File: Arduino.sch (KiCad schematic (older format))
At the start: 0 parts

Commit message: Arduino
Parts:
- added ARD?: ARDUINO_PINS, ~, symbol ARDUINO_PINS
- added R? (x13): R, ~, symbol R
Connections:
- net labels added: ADC_CS_N, CURR_MEAS, DAC_CS_N, GND, LED_EN_PWM, RELAY+, RELAY-, V+ADJ_MON, V-ADJ_MON
- net labels removed: CS_N, LED_EN, LED_FREQ, Relay+, Relay-
- wire segments 0 -> 27

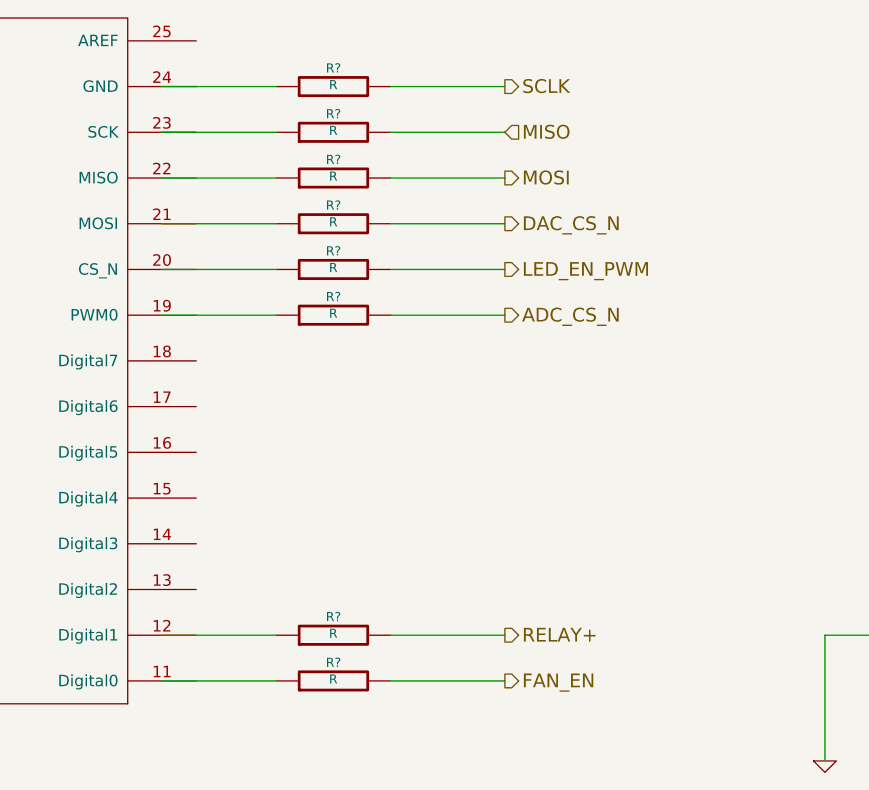
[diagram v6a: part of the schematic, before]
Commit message: Fan/Power refactoring
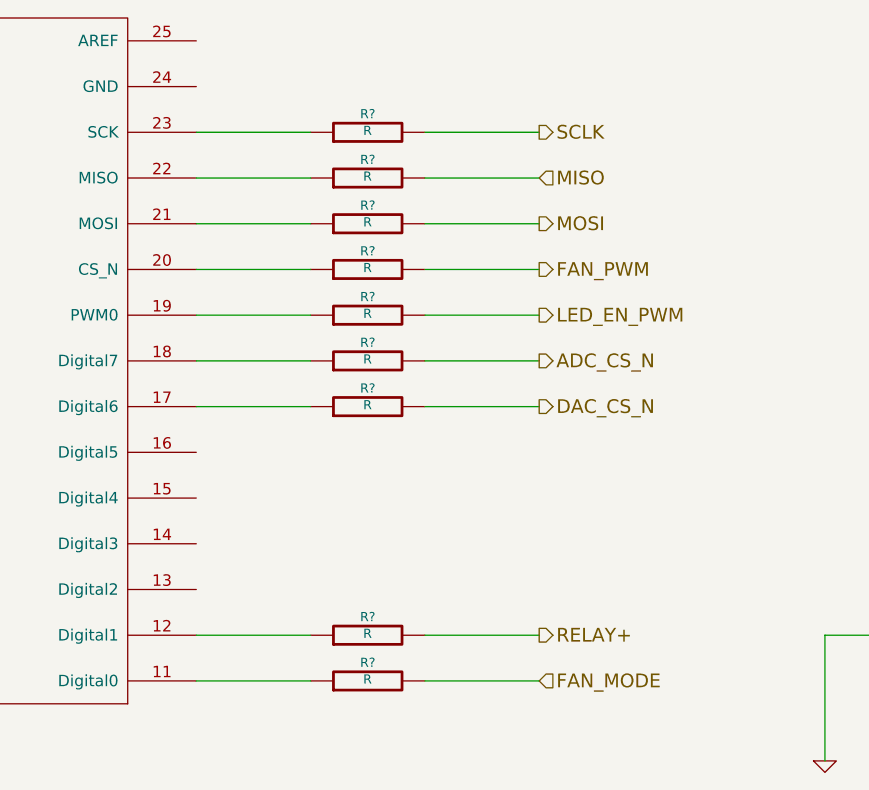
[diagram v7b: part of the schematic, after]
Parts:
- added R?: R, ~, symbol R
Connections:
- net labels added: FAN_MODE, FAN_PWM
- net labels removed: FAN_EN
- wire segments 27 -> 29
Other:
- moved on the sheet: R?
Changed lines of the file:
@@
 Comment4 ""
 $EndDescr
-Text HLabel 7450 3450 2    60   Output ~ 0
+Text HLabel 7600 3650 2    60   Output ~ 0
 MOSI
-Text HLabel 7450 3250 2    60   Input ~ 0
+Text HLabel 7600 3450 2    60   Input ~ 0
 MISO
-Text HLabel 7450 3050 2    60   Output ~ 0
+Text HLabel 7600 3250 2    60   Output ~ 0
 SCLK
-Text HLabel 7450 5450 2    60   Output ~ 0
+Text HLabel 7600 5450 2    60   Output ~ 0
 RELAY+
 Text HLabel 9900 5450 2    60   Output ~ 0
 RELAY-
-Text HLabel 7450 3650 2    60   Output ~ 0
-DAC_CS_N
-Text HLabel 7450 5650 2    60   Output ~ 0
-FAN_EN
+Text HLabel 7600 3850 2    60   Output ~ 0
+FAN_PWM
 Text HLabel 2850 5250 0    60   Input ~ 0
 TACH_MEAS
@@
 L R R?
 U 1 1 52F7405F
-P 6700 5650
-F 0 "R?" V 6780 5650 40  0000 C CNN
-F 1 "R" V 6707 5651 40  0000 C CNN
-F 2 "~" V 6630 5650 30  0000 C CNN
-F 3 "~" H 6700 5650 30  0000 C CNN
-	1    6700 5650
-	0    -1   -1   0
-$EndComp
-Wire Wire Line
-	5950 5650 6450 5650
-Wire Wire Line
-	6950 5650 7450 5650
+P 6850 5650
+F 0 "R?" V 6930 5650 40  0000 C CNN
+F 1 "R" V 6857 5651 40  0000 C CNN
+F 2 "~" V 6780 5650 30  0000 C CNN
+F 3 "~" H 6850 5650 30  0000 C CNN
+	1    6850 5650
+	0    -1   -1   0
+$EndComp
+Wire Wire Line
+	6100 5650 6600 5650
+Wire Wire Line
+	7100 5650 7600 5650
 $Comp
 L R R?
 U 1 1 52F742D4
-P 6700 5450
-F 0 "R?" V 6780 5450 40  0000 C CNN
-F 1 "R" V 6707 5451 40  0000 C CNN
-F 2 "~" V 6630 5450 30  0000 C CNN
-F 3 "~" H 6700 5450 30  0000 C CNN
-	1    6700 5450
-	0    -1   -1   0
-$EndComp
-Wire Wire Line
-	5950 5450 6450 5450
-Wire Wire Line
-	6950 5450 7450 5450
+P 6850 5450
+F 0 "R?" V 6930 5450 40  0000 C CNN
+F 1 "R" V 6857 5451 40  0000 C CNN
+F 2 "~" V 6780 5450 30  0000 C CNN
+F 3 "~" H 6850 5450 30  0000 C CNN
+	1    6850 5450
+	0    -1   -1   0
+$EndComp
+Wire Wire Line
+	6100 5450 6600 5450
+Wire Wire Line
+	7100 5450 7600 5450
 $Comp
 L R R?
@@
 L R R?
 U 1 1 52F75679
-P 6700 3050
-F 0 "R?" V 6780 3050 40  0000 C CNN
-F 1 "R" V 6707 3051 40  0000 C CNN
-F 2 "~" V 6630 3050 30  0000 C CNN
-F 3 "~" H 6700 3050 30  0000 C CNN
-	1    6700 3050
+P 6850 3250
+F 0 "R?" V 6930 3250 40  0000 C CNN
+F 1 "R" V 6857 3251 40  0000 C CNN
+F 2 "~" V 6780 3250 30  0000 C CNN
+F 3 "~" H 6850 3250 30  0000 C CNN
+	1    6850 3250
 	0    -1   -1   0
 $EndComp
@@
 L R R?
 U 1 1 52F75688
-P 6700 3250
-F 0 "R?" V 6780 3250 40  0000 C CNN
-F 1 "R" V 6707 3251 40  0000 C CNN
-F 2 "~" V 6630 3250 30  0000 C CNN
-F 3 "~" H 6700 3250 30  0000 C CNN
-	1    6700 3250
+P 6850 3450
+F 0 "R?" V 6930 3450 40  0000 C CNN
+F 1 "R" V 6857 3451 40  0000 C CNN
+F 2 "~" V 6780 3450 30  0000 C CNN
+F 3 "~" H 6850 3450 30  0000 C CNN
+	1    6850 3450
 	0    -1   -1   0
 $EndComp
@@
 L R R?
 U 1 1 52F75697
-P 6700 3450
-F 0 "R?" V 6780 3450 40  0000 C CNN
-F 1 "R" V 6707 3451 40  0000 C CNN
-F 2 "~" V 6630 3450 30  0000 C CNN
-F 3 "~" H 6700 3450 30  0000 C CNN
-	1    6700 3450
+P 6850 3650
+F 0 "R?" V 6930 3650 40  0000 C CNN
+F 1 "R" V 6857 3651 40  0000 C CNN
+F 2 "~" V 6780 3650 30  0000 C CNN
+F 3 "~" H 6850 3650 30  0000 C CNN
+	1    6850 3650
 	0    -1   -1   0
 $EndComp
@@
 L R R?
 U 1 1 52F756A6
-P 6700 3650
-F 0 "R?" V 6780 3650 40  0000 C CNN
-F 1 "R" V 6707 3651 40  0000 C CNN
-F 2 "~" V 6630 3650 30  0000 C CNN
-F 3 "~" H 6700 3650 30  0000 C CNN
-	1    6700 3650
-	0    -1   -1   0
-$EndComp
-Wire Wire Line
-	5950 3050 6450 3050
-Wire Wire Line
-	6950 3050 7450 3050
-Wire Wire Line
-	5950 3250 6450 3250
-Wire Wire Line
-	6950 3250 7450 3250
-Wire Wire Line
-	5950 3450 6450 3450
-Wire Wire Line
-	6950 3450 7450 3450
-Wire Wire Line
-	5950 3650 6450 3650
-Wire Wire Line
-	6950 3650 7450 3650
-Text HLabel 7450 3850 2    60   Output ~ 0
+P 6850 3850
+F 0 "R?" V 6930 3850 40  0000 C CNN
+F 1 "R" V 6857 3851 40  0000 C CNN
+F 2 "~" V 6780 3850 30  0000 C CNN
+F 3 "~" H 6850 3850 30  0000 C CNN
+	1    6850 3850
+	0    -1   -1   0
+$EndComp
+Wire Wire Line
+	6100 3250 6600 3250
+Wire Wire Line
+	7100 3250 7600 3250
+Wire Wire Line
+	6100 3450 6600 3450
+Wire Wire Line
+	7100 3450 7600 3450
+Wire Wire Line
+	6100 3650 6600 3650
+Wire Wire Line
+	7100 3650 7600 3650
+Wire Wire Line
+	6100 3850 6600 3850
+Wire Wire Line
+	7100 3850 7600 3850
+Text HLabel 7600 4050 2    60   Output ~ 0
 LED_EN_PWM
 $Comp
 L R R?
 U 1 1 52F7599A
-P 6700 3850
-F 0 "R?" V 6780 3850 40  0000 C CNN
-F 1 "R" V 6707 3851 40  0000 C CNN
-F 2 "~" V 6630 3850 30  0000 C CNN
-F 3 "~" H 6700 3850 30  0000 C CNN
-	1    6700 3850
-	0    -1   -1   0
-$EndComp
-Wire Wire Line
-	5950 3850 6450 3850
-Wire Wire Line
-	6950 3850 7450 3850
+P 6850 4050
+F 0 "R?" V 6930 4050 40  0000 C CNN
+F 1 "R" V 6857 4051 40  0000 C CNN
+F 2 "~" V 6780 4050 30  0000 C CNN
+F 3 "~" H 6850 4050 30  0000 C CNN
+	1    6850 4050
+	0    -1   -1   0
+$EndComp
+Wire Wire Line
+	6100 4050 6600 4050
+Wire Wire Line
+	7100 4050 7600 4050
 $Comp
 L R R?
@@
 	1    0    0    -1
 $EndComp
-Text HLabel 7450 4050 2    60   Output ~ 0
+Text HLabel 7600 4250 2    60   Output ~ 0
 ADC_CS_N
 $Comp
 L R R?
 U 1 1 52F63AB3
-P 6700 4050
-F 0 "R?" V 6780 4050 40  0000 C CNN
-F 1 "R" V 6707 4051 40  0000 C CNN
-F 2 "~" V 6630 4050 30  0000 C CNN
-F 3 "~" H 6700 4050 30  0000 C CNN
-	1    6700 4050
-	0    -1   -1   0
-$EndComp
-Wire Wire Line
-	5950 4050 6450 4050
-Wire Wire Line
-	6950 4050 7450 4050
+P 6850 4250
+F 0 "R?" V 6930 4250 40  0000 C CNN
+F 1 "R" V 6857 4251 40  0000 C CNN
+F 2 "~" V 6780 4250 30  0000 C CNN
+F 3 "~" H 6850 4250 30  0000 C CNN
+	1    6850 4250
+	0    -1   -1   0
+$EndComp
+Wire Wire Line
+	6100 4250 6600 4250
+Wire Wire Line
+	7100 4250 7600 4250
+Text HLabel 7600 5650 2    60   Input ~ 0
+FAN_MODE
+Text HLabel 7600 4450 2    60   Output ~ 0
+DAC_CS_N
+$Comp
+L R R?
+U 1 1 52F68416
+P 6850 4450
+F 0 "R?" V 6930 4450 40  0000 C CNN
+F 1 "R" V 6857 4451 40  0000 C CNN
+F 2 "~" V 6780 4450 30  0000 C CNN
+F 3 "~" H 6850 4450 30  0000 C CNN
+	1    6850 4450
+	0    -1   -1   0
+$EndComp
+Wire Wire Line
+	6100 4450 6600 4450
+Wire Wire Line
+	7100 4450 7600 4450
 $EndSCHEMATC
